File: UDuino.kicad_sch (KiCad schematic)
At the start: 10 parts, among them J101 Barrel_Jack, J102 PMOD1, J103 Conn_01x03_Male, J104 Conn_01x03_Male, J105 Conn_01x04_Male, J106 Conn_01x04_Male, U101 STM32L452VCTx

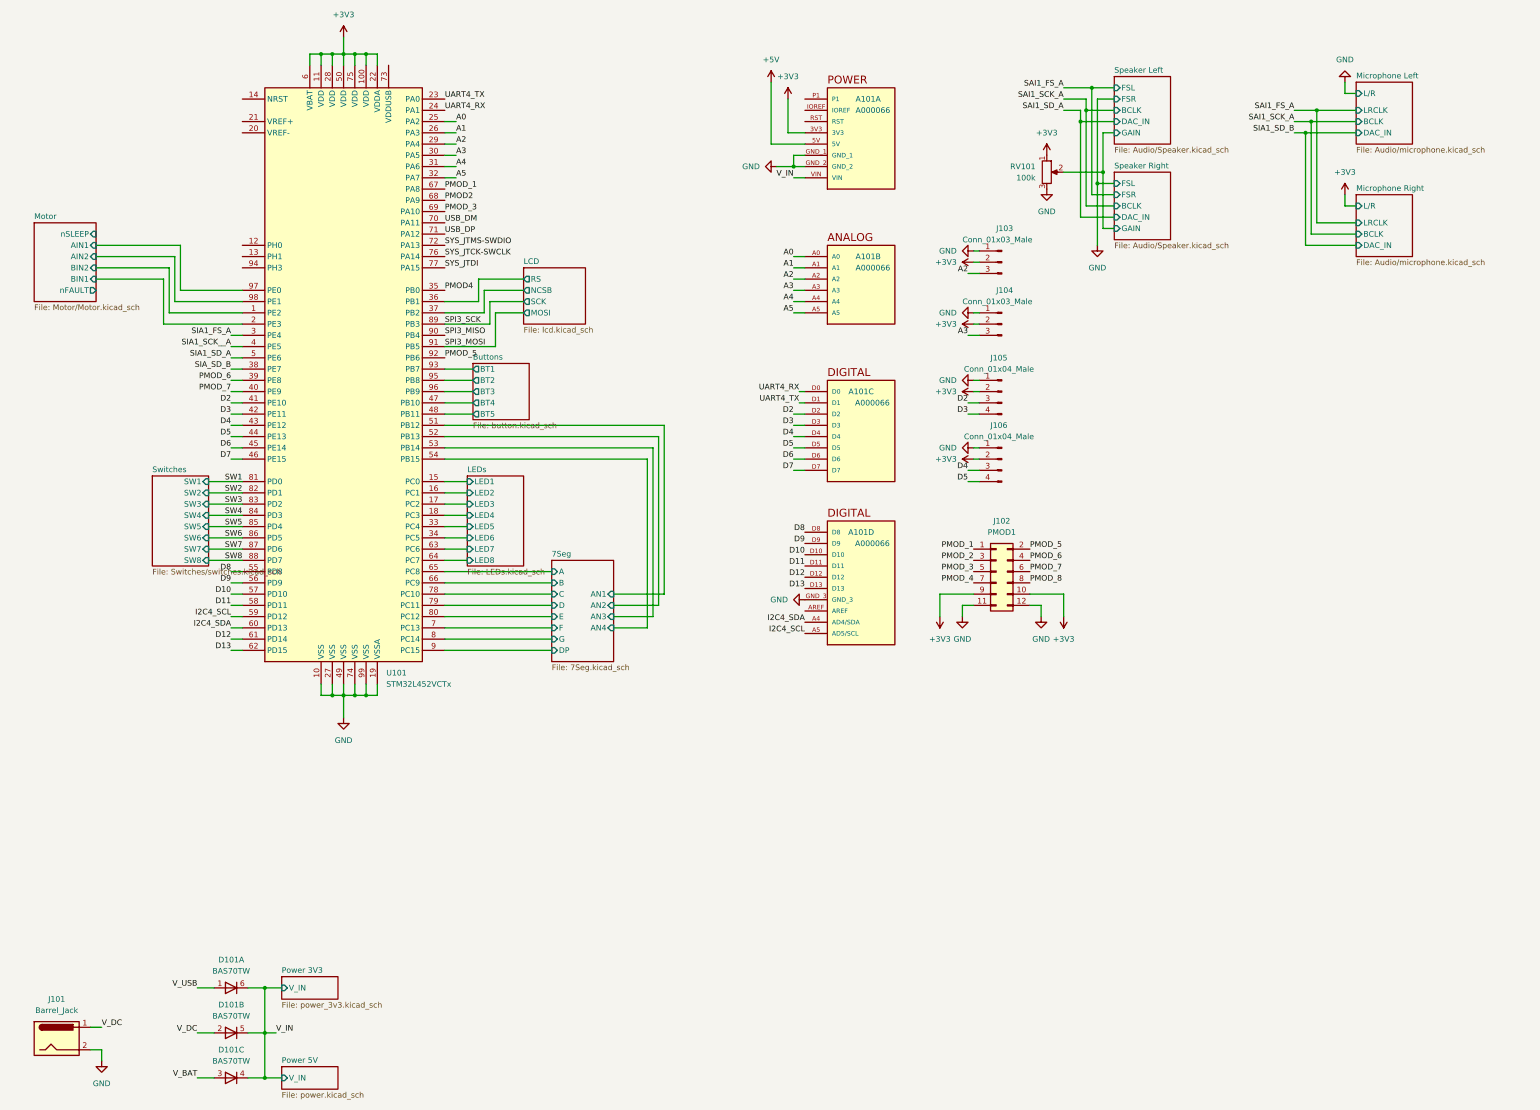
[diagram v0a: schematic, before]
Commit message: Weekend progress
Things that remain:
4 LEDs to Microcontroller
7-Seg to Microcontroller
LCD to Microcontroller
Microphone and Speakers to Microcontroller
Power circuitry
USB-C connector
Reset and Boot buttons
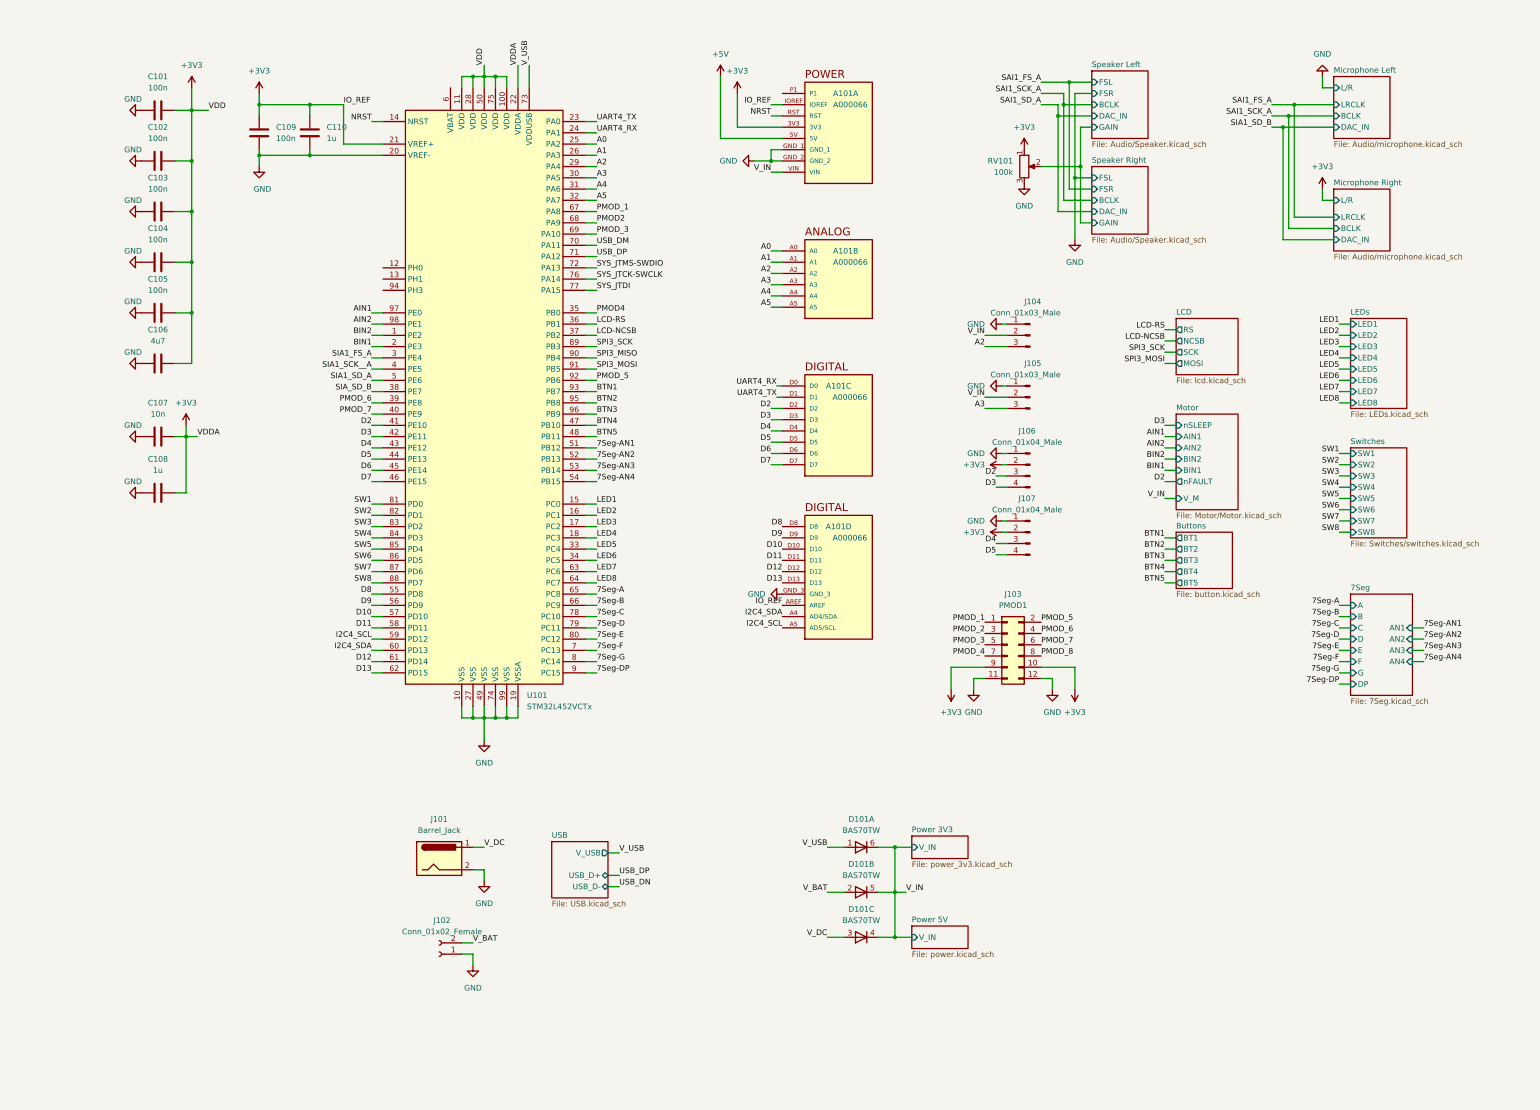
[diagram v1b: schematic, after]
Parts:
- added C101, C102, C103, C104, C105, C109: 100n, Capacitor_SMD:C_0805_2012Metric, symbol Device:C
- added C106: 4u7, Capacitor_SMD:C_0603_1608Metric, symbol Device:C
- added C107: 10n, Capacitor_SMD:C_0603_1608Metric, symbol Device:C
- added C108, C110: 1u, Capacitor_SMD:C_0603_1608Metric, symbol Device:C
- added J102: Conn_01x02_Female, Connector_JST:JST_XH_B2B-XH-AM_1x02_P2.50mm_Vertical, symbol Connector:Conn_01x02_Female
- renumbered J102 to J103, J103 to J104, J104 to J105, J105 to J106, J106 to J107
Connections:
- net +3V3: now also A101.AREF, A101.IOREF, U101.21 (VREF+), C101.2, C102.2, C103.2, C104.2, C105.2, C106.2, C107.2, C108.2, C109.1, C110.1; no longer J104.2 (Pin_2), J105.2 (Pin_2), U101.6 (VBAT)
- net GND: now also U101.20 (VREF-), C101.1, C102.1, C103.1, C104.1, C105.1, C106.1, C107.1, C108.1, C109.2, C110.2, J102.1 (Pin_1)
- net V_BAT: now also D101.2 (A), J102.2 (Pin_2); no longer D101.3 (A)
- net V_DC: now also D101.3 (A); no longer D101.2 (A)
- net V_IN: now also J104.2 (Pin_2), J105.2 (Pin_2)
- net V_USB: now also U101.73 (VDDUSB)
- net NRST: now reaches A101.RST
- net NRST: now also U101.14 (NRST)
- net 7Seg/A renamed 7Seg-A
- net 7Seg/AN1 renamed 7Seg-AN1
- net 7Seg/AN2 renamed 7Seg-AN2
- net 7Seg/AN3 renamed 7Seg-AN3
- net 7Seg/AN4 renamed 7Seg-AN4
- net 7Seg/B renamed 7Seg-B
- net 7Seg/C renamed 7Seg-C
- net 7Seg/D renamed 7Seg-D
- net 7Seg/DP renamed 7Seg-DP
- net 7Seg/E renamed 7Seg-E
- net 7Seg/F renamed 7Seg-F
- net 7Seg/G renamed 7Seg-G
- net Buttons/BT1 renamed BTN1
- net Buttons/BT2 renamed BTN2
- net Buttons/BT3 renamed BTN3
- net Buttons/BT4 renamed BTN4
- net Buttons/BT5 renamed BTN5
- net LCD/NCSB renamed LCD-NCSB
- net LCD/RS renamed LCD-RS
- net LEDs/LED1 renamed LED1
- net LEDs/LED2 renamed LED2
- net LEDs/LED3 renamed LED3
- net LEDs/LED4 renamed LED4
- net LEDs/LED5 renamed LED5
- net LEDs/LED6 renamed LED6
- net LEDs/LED7 renamed LED7
- net LEDs/LED8 renamed LED8
- net Motor/AIN1 renamed AIN1
- net Motor/AIN2 renamed AIN2
- net Motor/BIN1 renamed BIN1
- net Motor/BIN2 renamed BIN2
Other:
- added sheet USB (USB.kicad_sch)
- sheet Motor ports: added V_M; removed none
- moved on the sheet: A101A, A101B, A101C, A101D, D101A, D101B, D101C, J101, J103, J104, J105, J106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

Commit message: Feb 12 2023 Week Work
Remaining Things to accomplish
Audio connect to Microcontroller
7-Seg connect to Microcontroller
PMOD connect to Microcontroller
Misc Microcontroller items, like reset and boot buttons
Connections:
- net SIA1_FS_A is gone; now on net SAI1_FS_A: U101.3 (PE4)
- net SIA1_SD_A is gone; now on net SAI1_SD_A: U101.5 (PE6)
- net USB_DM is gone; now on net USB_DN: U101.70 (PA11)
- net SIA1_SCK__A renamed SAI1_SCK__A
- net SIA_SD_B renamed SAI_SD_B
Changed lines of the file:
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@@
     (stroke (width 0) (type default) (color 0 0 0 0))
   )
-  (wire (pts (xy 280.67 124.46) (xy 283.21 124.46))
+  (wire (pts (xy 280.67 123.19) (xy 283.21 123.19))
     (stroke (width 0) (type default) (color 0 0 0 0))
   )
@@
     (effects (font (size 1.27 1.27)) (justify right bottom))
   )
-  (label "SIA1_SD_A" (at 101.6 97.79 180)
+  (label "SAI1_SD_A" (at 101.6 97.79 180)
     (effects (font (size 1.27 1.27)) (justify right bottom))
   )
@@
     (effects (font (size 1.27 1.27)) (justify right bottom))
   )
-  (label "SIA1_SCK__A" (at 101.6 95.25 180)
+  (label "SAI1_SCK__A" (at 101.6 95.25 180)
     (effects (font (size 1.27 1.27)) (justify right bottom))
   )
@@
     (effects (font (size 1.27 1.27)) (justify right bottom))
   )
-  (label "SIA1_FS_A" (at 101.6 92.71 180)
+  (label "SAI1_FS_A" (at 101.6 92.71 180)
     (effects (font (size 1.27 1.27)) (justify right bottom))
   )
@@
     (effects (font (size 1.27 1.27)) (justify left bottom))
   )
-  (label "SIA_SD_B" (at 101.6 100.33 180)
+  (label "SAI_SD_B" (at 101.6 100.33 180)
     (effects (font (size 1.27 1.27)) (justify right bottom))
   )
@@
     (effects (font (size 1.27 1.27)) (justify left bottom))
   )
-  (label "USB_DM" (at 152.4 67.31 0)
+  (label "USB_DN" (at 152.4 67.31 0)
     (effects (font (size 1.27 1.27)) (justify left bottom))
   )
@@
     (effects (font (size 1.27 1.27)) (justify left bottom))
   )
-  (label "V_IN" (at 280.67 124.46 180)
+  (label "V_IN" (at 280.67 123.19 180)
     (effects (font (size 1.27 1.27)) (justify right bottom))
   )
@@
     )
   )
-  (sheet (at 283.21 105.41) (size 13.97 21.59) (fields_autoplaced)
+  (sheet (at 283.21 105.41) (size 13.97 20.32) (fields_autoplaced)
     (stroke (width 0.1524) (type solid) (color 0 0 0 0))
     (fill (color 0 0 0 0.0000))
@@
       (effects (font (size 1.27 1.27)) (justify left bottom))
     )
-    (property "Sheet file" "Motor/Motor.kicad_sch" (id 1) (at 283.21 127.5846 0)
+    (property "Sheet file" "Motor/Motor.kicad_sch" (id 1) (at 283.21 126.3146 0)
       (effects (font (size 1.27 1.27)) (justify left top))
     )
@@
       (effects (font (size 1.27 1.27)) (justify left))
     )
-    (pin "V_M" input (at 283.21 124.46 180)
-      (effects (font (size 1.27 1.27)) (justify left))
-    )
+    (pin "V_M" input (at 283.21 123.19 180)
+      (effects (font (size 1.27 1.27)) (justify left))
+    )

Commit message: REVISION 0 DONE
Done first revision of the UDUINO
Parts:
- removed C110: 1u, Capacitor_SMD:C_0603_1608Metric, symbol Device:C
- removed U101: STM32L452VCTx, Package_QFP:LQFP-100_14x14mm_P0.5mm, symbol MCU_ST_STM32L4:STM32L452VCTx
- added R101: 10k, Resistor_SMD:R_0603_1608Metric, symbol Device:R
- added S101, S102: PTS636_SM43_SMTR_LFS, PTS636SM43SMTRLFS, symbol PTS636_SM43_SMTR_LFS:PTS636_SM43_SMTR_LFS
- added U101: STM32F072VBTx, Package_QFP:LQFP-100_14x14mm_P0.5mm, symbol MCU_ST_STM32F0:STM32F072VBTx
- C105, C109: value 100n -> 4u7; footprint Capacitor_SMD:C_0805_2012Metric -> Capacitor_SMD:C_0603_1608Metric; Manufacturer_Part_Number CL21B104KCFNNNE -> CL10A475KO8NNNC
- C107: value 10n -> 100n; footprint Capacitor_SMD:C_0603_1608Metric -> Capacitor_SMD:C_0805_2012Metric; Manufacturer_Part_Number 0603B103K500NT -> CL21B104KCFNNNE
- C108: value 1u -> 100n; footprint Capacitor_SMD:C_0603_1608Metric -> Capacitor_SMD:C_0805_2012Metric; Manufacturer_Part_Number CL10A105KB8NNNC -> CL21B104KCFNNNE
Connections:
- net +3V3: now also C109.2, S101.2 (NO), U101.100 (VDD), U101.21 (VDDA), U101.28 (VDD), U101.50 (VDD), U101.75 (VDDIO2); no longer C101.2, C109.1
- net 7Seg-A: now also U101.33 (PC4)
- net 7Seg-AN1: now also U101.23 (PA0)
- net 7Seg-AN2: now also U101.24 (PA1)
- net 7Seg-AN3: now also U101.25 (PA2)
- net 7Seg-AN4: now also U101.26 (PA3)
- net 7Seg-B: now also U101.34 (PC5)
- net 7Seg-C: now also U101.35 (PB0)
- net 7Seg-D: now also U101.36 (PB1)
- net 7Seg-DP: now also U101.40 (PE9)
- net 7Seg-E: now also U101.37 (PB2)
- net 7Seg-F: now also U101.38 (PE7)
- net 7Seg-G: now also U101.39 (PE8)
- net A0: now also U101.78 (PC10)
- net A1: now also U101.79 (PC11)
- net A2: now also U101.80 (PC12)
- net A3: now also U101.31 (PA6)
- net A4: now also U101.41 (PE10)
- net A5: now also U101.53 (PB14)
- net AIN1: now also U101.68 (PA9)
- net AIN2: now also U101.69 (PA10)
- net BIN1: now also U101.73 (PF6)
- net BIN2: now also U101.72 (PA13)
- net BTN1: now also U101.89 (PB3)
- net BTN2: now also U101.90 (PB4)
- net BTN3: now also U101.91 (PB5)
- net BTN4: now also U101.95 (PB8)
- net BTN5: now also U101.96 (PB9)
- net D10: now also U101.63 (PC6)
- net D11: now also U101.64 (PC7)
- net D12: now also U101.65 (PC8)
- net D13: now also U101.66 (PC9)
- net D2: now also J106.4 (Pin_4), U101.55 (PD8); no longer J106.3 (Pin_3)
- net D3: now also J106.3 (Pin_3), U101.56 (PD9); no longer J106.4 (Pin_4)
- net D4: now also J107.4 (Pin_4), U101.57 (PD10); no longer J107.3 (Pin_3)
- net D5: now also J107.3 (Pin_3), U101.58 (PD11); no longer J107.4 (Pin_4)
- net D6: now also U101.59 (PD12)
- net D7: now also U101.60 (PD13)
- net D8: now also U101.61 (PD14)
- net D9: now also U101.62 (PD15)
- net GND: now also C109.1, R101.2, S102.2 (NO), U101.20 (VSSA), U101.27 (VSS), U101.49 (VSS), U101.74 (VSS), U101.99 (VSS); no longer C109.2
- net LCD-NCSB: now also U101.43 (PE12)
- net LCD-RS: now also U101.42 (PE11)
- net LED1: now also U101.97 (PE0)
- net LED2: now also U101.98 (PE1)
- net LED3: now also U101.1 (PE2)
- net LED4: now also U101.2 (PE3)
- net LED5: now also U101.3 (PE4)
- net LED6: now also U101.4 (PE5)
- net LED7: now also U101.5 (PE6)
- net LED8: now also U101.7 (PC13)
- net NRST: now also C101.2, S102.1 (COM), U101.14 (NRST)
- net PMOD_1: now also U101.22 (PF3)
- net PMOD_2: now also U101.19 (PF2)
- net PMOD_3: now also U101.18 (PC3)
- net PMOD_4: now also U101.17 (PC2)
- net PMOD_5: now also U101.16 (PC1)
- net PMOD_6: now also U101.15 (PC0)
- net PMOD_7: now also U101.11 (PF10)
- net PMOD_8: now also U101.10 (PF9)
- net SW1: now also U101.81 (PD0)
- net SW2: now also U101.82 (PD1)
- net SW3: now also U101.83 (PD2)
- net SW4: now also U101.84 (PD3)
- net SW5: now also U101.85 (PD4)
- net SW6: now also U101.86 (PD5)
- net SW7: now also U101.87 (PD6)
- net SW8: now also U101.88 (PD7)
- net USB_DN: now also U101.70 (PA11)
- net USB_DP: now also U101.71 (PA12)
- removed net I2C4_SCL: A101.A5 (AD5/SCL)
- removed net I2C4_SDA: A101.A4 (AD4/SDA)
- net UART4_RX renamed UART_RX
- net UART_RX: now also U101.48 (PB11)
- net UART4_TX renamed UART_TX
- net UART_TX: now also U101.47 (PB10)
- new net BOOT: R101.1, S101.1 (COM), U101.94 (BOOT0)
- new net I2C1_SCL: A101.SCL (AD5/SCL), U101.93 (PB7)
- new net I2C1_SDA: A101.SDA (AD4/SDA), U101.92 (PB6)
- new net I2S1_CK: U101.30 (PA5)
- new net I2S1_SD: U101.32 (PA7)
- new net I2S1_WS: U101.29 (PA4)
- new net I2S2_CK: U101.52 (PB13)
- new net I2S2_SD: U101.54 (PB15)
- new net I2S2_WS: U101.51 (PB12)
- new net NFAULT: U101.76 (PA14)
- new net NSLEEP: U101.67 (PA8)
- new net SPI1_MISO: U101.45 (PE14)
- new net SPI1_MOSI: U101.46 (PE15)
- new net SPI1_SCK: U101.44 (PE13)
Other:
- moved on the sheet: J104, J105, J106, J107

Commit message: Update BOM and POC files
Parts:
- RV101: Manufacturer_Name (none) -> Bourns Inc.; Manufacturer_Part_Number (none) -> 3352T-1-104LF
- U101: Manufacturer_Name (none) -> STMicroelectronics; Manufacturer_Part_Number (none) -> STM32F072VBT6
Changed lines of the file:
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@@
+      (effects (font (size 1.27 1.27)) hide)
+    )
+    (property "Manufacturer_Name" "Bourns Inc." (id 4) (at 248.92 49.53 0)
+      (effects (font (size 1.27 1.27)) hide)
+    )
+    (property "Manufacturer_Part_Number" "3352T-1-104LF" (id 5) (at 248.92 49.53 0)
       (effects (font (size 1.27 1.27)) hide)
     )
@@
     )
     (property "Datasheet" "http://www.st.com/st-web-ui/static/active/en/resource/technical/document/datasheet/DM00090510.pdf" (id 3) (at 127 100.33 0)
+      (effects (font (size 1.27 1.27)) hide)
+    )
+    (property "Manufacturer_Name" "STMicroelectronics" (id 4) (at 127 100.33 0)
+      (effects (font (size 1.27 1.27)) hide)
+    )
+    (property "Manufacturer_Part_Number" "STM32F072VBT6" (id 5) (at 127 100.33 0)
       (effects (font (size 1.27 1.27)) hide)
     )
@@
     )
     (path "/74114fa7-3930-46b1-8d47-2b12a2f25cb0/a3c26ba8-ef7e-4a30-abe2-d3286603d2cc"
-      (reference "Q901") (unit 1) (value "TRANS_PNP-MMBT4403") (footprint "Package_TO_SOT_SMD:SOT-23")
+      (reference "Q901") (unit 1) (value "SMMBT4403LT1G") (footprint "Package_TO_SOT_SMD:SOT-23")
     )
     (path "/74114fa7-3930-46b1-8d47-2b12a2f25cb0/7bb024ab-a972-4cce-8add-295a0f45f466"
-      (reference "Q902") (unit 1) (value "TRANS_PNP-MMBT4403") (footprint "Package_TO_SOT_SMD:SOT-23")
+      (reference "Q902") (unit 1) (value "SMMBT4403LT1G") (footprint "Package_TO_SOT_SMD:SOT-23")
     )
     (path "/74114fa7-3930-46b1-8d47-2b12a2f25cb0/694c7da1-bce2-4c1f-a0e5-8ae0f533e3dd"
-      (reference "Q903") (unit 1) (value "TRANS_PNP-MMBT4403") (footprint "Package_TO_SOT_SMD:SOT-23")
+      (reference "Q903") (unit 1) (value "SMMBT4403LT1G") (footprint "Package_TO_SOT_SMD:SOT-23")
     )
     (path "/74114fa7-3930-46b1-8d47-2b12a2f25cb0/20444a69-7f02-4c08-a8ed-26c292138af5"
-      (reference "Q904") (unit 1) (value "TRANS_PNP-MMBT4403") (footprint "Package_TO_SOT_SMD:SOT-23")
+      (reference "Q904") (unit 1) (value "SMMBT4403LT1G") (footprint "Package_TO_SOT_SMD:SOT-23")
     )
     (path "/2ddc27b1-935f-4494-9a1d-a725c1f189ca"
